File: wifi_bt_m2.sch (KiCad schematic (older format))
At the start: 25 parts, among them J1502 M.2_Key_E, Q1501 FDV301N, Q1502 FDV301N, SW1501 WWAN_HKS, U1502 74AUP2G08, U1504 NTB0104GU12, U1702 NTB0104GU12

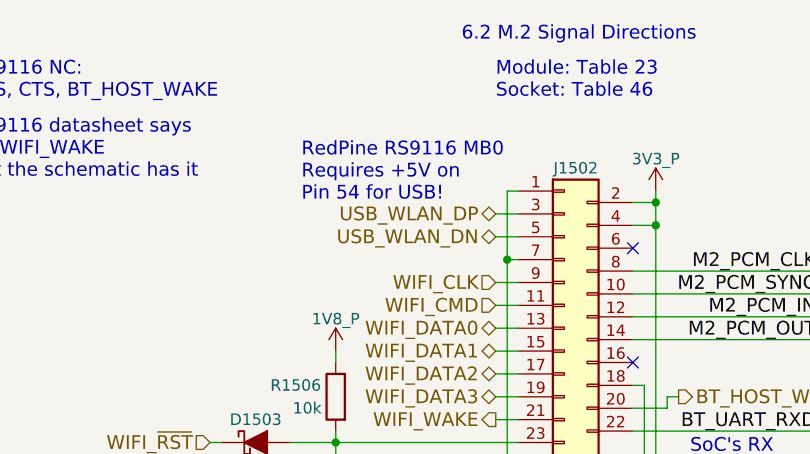
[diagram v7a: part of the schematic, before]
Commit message: Include power load switch ICs to the 3.3V and 5V rails so that the SoC can disable the peripherals' power using the PWR_EN signal
Need to verify that 3V3's capacitance is greater than 3V3_P!

Next step is to have PWR_EN control the various logic translator chips EN pins.
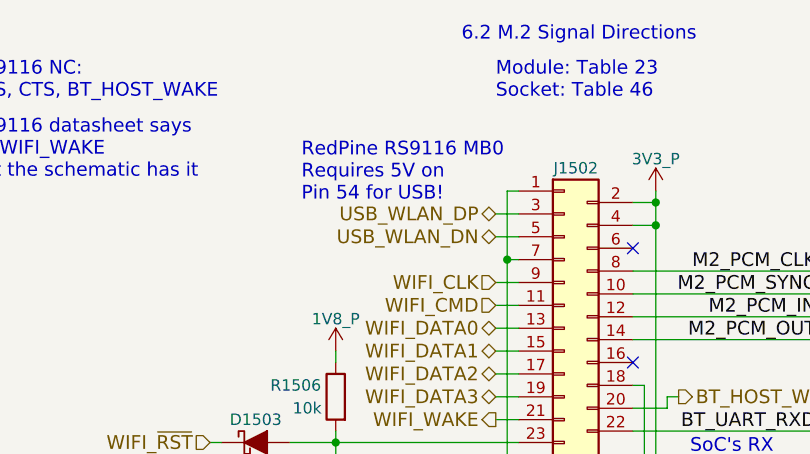
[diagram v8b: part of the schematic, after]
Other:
- note added: "RedPine RS9116 MB0\nRequires 5V on\nPin 54 for USB!"
- note removed: "RedPine RS9116 MB0\nRequires +5V on\nPin 54 for USB!"
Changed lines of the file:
@@
 	5350 1500 5250 1500
 $Comp
-L GND #PWR0256
+L GND #PWR0275
 U 1 1 5B01D9F9
 P 5300 5050
-F 0 "#PWR0256" H 5300 4800 50  0001 C CNN
+F 0 "#PWR0275" H 5300 4800 50  0001 C CNN
 F 1 "GND" H 5300 4900 50  0000 C CNN
 F 2 "" H 5300 5050 50  0001 C CNN
@@
 Connection ~ 5300 5000
 $Comp
-L GND #PWR0257
+L GND #PWR0276
 U 1 1 5B01E5BE
 P 5900 5050
-F 0 "#PWR0257" H 5900 4800 50  0001 C CNN
+F 0 "#PWR0276" H 5900 4800 50  0001 C CNN
 F 1 "GND" H 5900 4900 50  0000 C CNN
 F 2 "" H 5900 5050 50  0001 C CNN
@@
 	5900 2150 5900 5050
 $Comp
-L 3V3_P #PWR0258
+L 3V3_P #PWR0277
 U 1 1 5B01E6B8
 P 5950 1300
-F 0 "#PWR0258" H 5950 1150 50  0001 C CNN
+F 0 "#PWR0277" H 5950 1150 50  0001 C CNN
 F 1 "3V3_P" H 5950 1440 50  0000 C CNN
 F 2 "" H 5950 1300 50  0001 C CNN
@@
 $EndComp
 $Comp
-L 3V3_P #PWR0259
+L 3V3_P #PWR0278
 U 1 1 5B0C3C8A
 P 10150 3900
-F 0 "#PWR0259" H 10150 3750 50  0001 C CNN
+F 0 "#PWR0278" H 10150 3750 50  0001 C CNN
 F 1 "3V3_P" H 10150 4040 50  0000 C CNN
 F 2 "" H 10150 3900 50  0001 C CNN
@@
 NoConn ~ 6500 3750
 $Comp
-L 3V3_P #PWR0260
+L 3V3_P #PWR0279
 U 1 1 5B0D90EE
 P 7750 3300
-F 0 "#PWR0260" H 7750 3150 50  0001 C CNN
+F 0 "#PWR0279" H 7750 3150 50  0001 C CNN
 F 1 "3V3_P" H 7750 3440 50  0000 C CNN
 F 2 "" H 7750 3300 50  0001 C CNN
@@
 	7750 3300 7750 3350
 $Comp
-L GND #PWR0261
+L GND #PWR0280
 U 1 1 5B0D91C5
 P 7750 4700
-F 0 "#PWR0261" H 7750 4450 50  0001 C CNN
+F 0 "#PWR0280" H 7750 4450 50  0001 C CNN
 F 1 "GND" H 7750 4550 50  0000 C CNN
 F 2 "" H 7750 4700 50  0001 C CNN
@@
 Connection ~ 4550 2400
 $Comp
-L 1V8_P #PWR0262
+L 1V8_P #PWR0281
 U 1 1 5AEFAF82
 P 4550 2000
-F 0 "#PWR0262" H 4550 1850 50  0001 C CNN
+F 0 "#PWR0281" H 4550 1850 50  0001 C CNN
 F 1 "1V8_P" H 4550 2140 50  0000 C CNN
 F 2 "" H 4550 2000 50  0001 C CNN
@@
 $EndComp
 $Comp
-L 1V8_P #PWR0263
+L 1V8_P #PWR0282
 U 1 1 5AEB9155
 P 7000 5050
-F 0 "#PWR0263" H 7000 4900 50  0001 C CNN
+F 0 "#PWR0282" H 7000 4900 50  0001 C CNN
 F 1 "1V8_P" H 7000 5190 50  0000 C CNN
 F 2 "" H 7000 5050 50  0001 C CNN
@@
 TODO!!!\nverify if translators\nwith PWR_EN is needed!
 $Comp
-L 3V3_P #PWR0264
+L 3V3_P #PWR0283
 U 1 1 5AF2CD0D
 P 7750 4200
-F 0 "#PWR0264" H 7750 4050 50  0001 C CNN
+F 0 "#PWR0283" H 7750 4050 50  0001 C CNN
 F 1 "3V3_P" H 7750 4340 50  0000 C CNN
 F 2 "" H 7750 4200 50  0001 C CNN
@@
 	7750 4200 7750 4250
 $Comp
-L GND #PWR0265
+L GND #PWR0284
 U 1 1 5AF2CDB4
 P 7750 3800
-F 0 "#PWR0265" H 7750 3550 50  0001 C CNN
+F 0 "#PWR0284" H 7750 3550 50  0001 C CNN
 F 1 "GND" H 7750 3650 50  0000 C CNN
 F 2 "" H 7750 3800 50  0001 C CNN
@@
 $EndComp
 $Comp
-L GND #PWR0266
+L GND #PWR0285
 U 1 1 5AF3C984
 P 9000 4500
-F 0 "#PWR0266" H 9000 4250 50  0001 C CNN
+F 0 "#PWR0285" H 9000 4250 50  0001 C CNN
 F 1 "GND" H 9000 4350 50  0000 C CNN
 F 2 "" H 9000 4500 50  0001 C CNN
@@
 $EndComp
 $Comp
-L GND #PWR0267
+L GND #PWR0286
 U 1 1 5AF3C98A
 P 9500 4500
-F 0 "#PWR0267" H 9500 4250 50  0001 C CNN
+F 0 "#PWR0286" H 9500 4250 50  0001 C CNN
 F 1 "GND" H 9500 4350 50  0000 C CNN
 F 2 "" H 9500 4500 50  0001 C CNN
@@
 $EndComp
 $Comp
-L 1V8_P #PWR0268
+L 1V8_P #PWR0287
 U 1 1 5AEBC081
 P 9400 5050
-F 0 "#PWR0268" H 9400 4900 50  0001 C CNN
+F 0 "#PWR0287" H 9400 4900 50  0001 C CNN
 F 1 "1V8_P" H 9400 5190 50  0000 C CNN
 F 2 "" H 9400 5050 50  0001 C CNN
@@
 $EndComp
 $Comp
-L GND #PWR0269
+L GND #PWR0288
 U 1 1 5B2489BD
 P 6350 6200
-F 0 "#PWR0269" H 6350 5950 50  0001 C CNN
+F 0 "#PWR0288" H 6350 5950 50  0001 C CNN
 F 1 "GND" H 6350 6050 50  0000 C CNN
 F 2 "" H 6350 6200 50  0001 C CNN
@@
 $EndComp
 $Comp
-L GND #PWR0270
+L GND #PWR0289
 U 1 1 5B2489DB
 P 4600 6200
-F 0 "#PWR0270" H 4600 5950 50  0001 C CNN
+F 0 "#PWR0289" H 4600 5950 50  0001 C CNN
 F 1 "GND" H 4600 6050 50  0000 C CNN
 F 2 "" H 4600 6200 50  0001 C CNN
@@
 	4450 5750 5300 5750
 $Comp
-L GND #PWR0271
+L GND #PWR0290
 U 1 1 5B2489F2
 P 5400 7550
-F 0 "#PWR0271" H 5400 7300 50  0001 C CNN
+F 0 "#PWR0290" H 5400 7300 50  0001 C CNN
 F 1 "GND" H 5400 7400 50  0000 C CNN
 F 2 "" H 5400 7550 50  0001 C CNN
@@
 BCLK
 $Comp
-L 3V3_P #PWR0272
+L 3V3_P #PWR0291
 U 1 1 5B248A11
 P 6200 5700
-F 0 "#PWR0272" H 6200 5550 50  0001 C CNN
+F 0 "#PWR0291" H 6200 5550 50  0001 C CNN
 F 1 "3V3_P" H 6200 5840 50  0000 C CNN
 F 2 "" H 6200 5700 50  0001 C CNN
@@
 $EndComp
 $Comp
-L 1V8_P #PWR0273
+L 1V8_P #PWR0292
 U 1 1 5B248A1D
 P 4950 5700
-F 0 "#PWR0273" H 4950 5550 50  0001 C CNN
+F 0 "#PWR0292" H 4950 5550 50  0001 C CNN
 F 1 "1V8_P" H 4950 5840 50  0000 C CNN
 F 2 "" H 4950 5700 50  0001 C CNN
@@
 $EndComp
 $Comp
-L GND #PWR0274
+L GND #PWR0293
 U 1 1 5B337EDE
 P 3200 6200
-F 0 "#PWR0274" H 3200 5950 50  0001 C CNN
+F 0 "#PWR0293" H 3200 5950 50  0001 C CNN
 F 1 "GND" H 3200 6050 50  0000 C CNN
 F 2 "" H 3200 6200 50  0001 C CNN
@@
 $EndComp
 $Comp
-L GND #PWR0275
+L GND #PWR0294
 U 1 1 5B337EFC
 P 1450 6200
-F 0 "#PWR0275" H 1450 5950 50  0001 C CNN
+F 0 "#PWR0294" H 1450 5950 50  0001 C CNN
 F 1 "GND" H 1450 6050 50  0000 C CNN
 F 2 "" H 1450 6200 50  0001 C CNN
@@
 	1300 5750 2150 5750
 $Comp
-L GND #PWR0276
+L GND #PWR0295
 U 1 1 5B337F13
 P 2250 7550
-F 0 "#PWR0276" H 2250 7300 50  0001 C CNN
+F 0 "#PWR0295" H 2250 7300 50  0001 C CNN
 F 1 "GND" H 2250 7400 50  0000 C CNN
 F 2 "" H 2250 7550 50  0001 C CNN
@@
 	2650 7100 2700 7100
 $Comp
-L 3V3_P #PWR0277
+L 3V3_P #PWR0296
 U 1 1 5B337F23
 P 3050 5700
-F 0 "#PWR0277" H 3050 5550 50  0001 C CNN
+F 0 "#PWR0296" H 3050 5550 50  0001 C CNN
 F 1 "3V3_P" H 3050 5840 50  0000 C CNN
 F 2 "" H 3050 5700 50  0001 C CNN
@@
 $EndComp
 $Comp
-L 1V8_P #PWR0278
+L 1V8_P #PWR0297
 U 1 1 5B337F29
 P 1800 5700
-F 0 "#PWR0278" H 1800 5550 50  0001 C CNN
+F 0 "#PWR0297" H 1800 5550 50  0001 C CNN
 F 1 "1V8_P" H 1800 5840 50  0000 C CNN
 F 2 "" H 1800 5700 50  0001 C CNN
@@
 TODO:\nPin 54 on RS9116 is USB_VBUS Sink!!!
 Text Notes 4400 1350 0    60   ~ 0
-RedPine RS9116 MB0\nRequires +5V on\nPin 54 for USB!
+RedPine RS9116 MB0\nRequires 5V on\nPin 54 for USB!
 Text Notes 2950 1250 0    60   ~ 0
 RS9116 datasheet says\nno WIFI_WAKE\nbut the schematic has it
